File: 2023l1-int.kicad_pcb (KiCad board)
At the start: 2 copper layers, 185 x 188.1 mm, 134 parts, among them IC1 STM32F103CBTx, IC2 SN74LVC2G04DBVTG4, IC3 SN74LVC2G04DBVTG4, J1 52610-1433, J2 XT30, J3 PGMR, J4 FL, J5 FR, J6 BL, J7 BR, J8 XT60, Q1 STP75NF75, Q2 AO3400A, SW1 STM RST, SW2 L SW, SW3 M SW, U2 CD74HC4067SM, U4 CD74HC4067SM, U5 VNH5050A-E, U6 VNH5050A-E, U7 VNH5050A-E, U8 VNH5050A-E, Y1 8Mhz

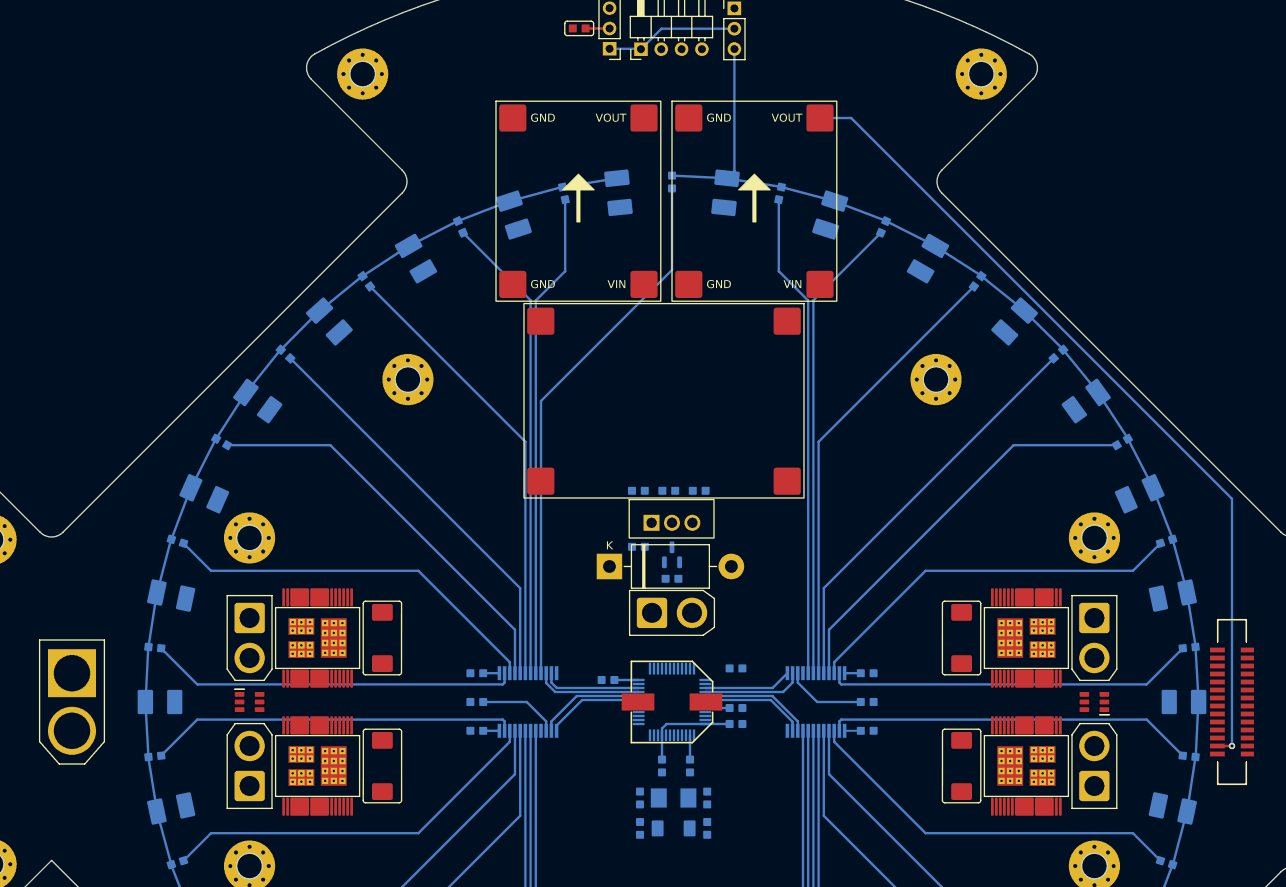
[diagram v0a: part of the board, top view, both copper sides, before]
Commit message: stm32 wiring done
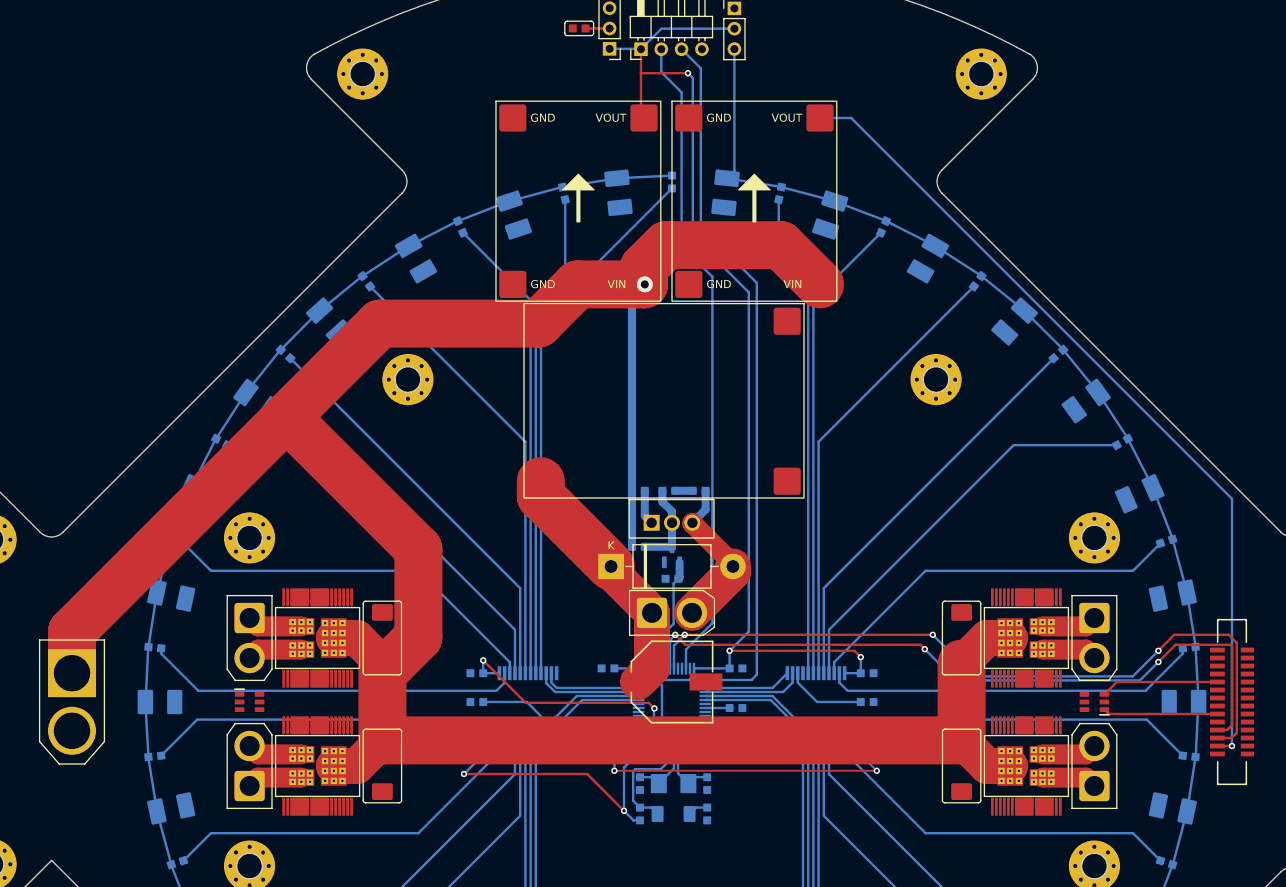
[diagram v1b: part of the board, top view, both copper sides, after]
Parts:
- moved C11 2.50 mm to (113.7, 103.5), turned to 0 degrees
- moved C14 2.37 mm to (110.7, 112.4), turned to 180 degrees
- moved D3 1.86 mm to (116.7, 112.3), turned to 180 degrees
- moved C4 1.80 mm to (118.1, 116.2)
- moved C5 1.80 mm to (109.7, 116.2)
- moved R41 1.80 mm to (118.1, 120.0)
- moved R45 1.80 mm to (109.7, 120.0)
- moved SW1 1.80 mm to (113.9, 120.0)
- moved Y1 1.80 mm to (113.9, 116.2)
- moved C12 1.45 mm to (105.7, 101.8)
- moved D2 0.20 mm to (106.1, 89.1)
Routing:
- net +12V: track 0.00 -> 316.8 mm, vias 0 -> 1
- net +3V3: track 36.3 -> 208.6 mm, vias 0 -> 5
- net /TX: track 0.00 -> 92.5 mm, vias 0 -> 3
- net /RX: track 0.00 -> 90.3 mm, vias 0 -> 3
- net /SWCLK: track 0.00 -> 88.8 mm
- net /SWDIO: track 0.00 -> 81.9 mm
- net /M1: track 2.03 -> 49.2 mm, vias 0 -> 2
- net +48V: track 0.00 -> 31.6 mm
- net /M2: track 2.02 -> 30.9 mm, vias 0 -> 2
- net Net-(D2-A): track 0.00 -> 20.2 mm
- net /RST: track 0.00 -> 15.7 mm
- net /BL DIR: track 0.00 -> 14.8 mm
- net /FL DIR: track 0.00 -> 14.4 mm
- net /Sol: track 0.00 -> 14.0 mm
- net Net-(Q2-D): track 0.00 -> 11.0 mm
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
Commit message: time to do it again
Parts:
- removed C16, C17, C18, C19: 220u, footprints:EIA-7343-D
- removed J4: FL, footprints:AMASS_XT30-F
- removed J5: FR, footprints:AMASS_XT30-F
- removed J6: BL, footprints:AMASS_XT30-F
- removed J7: BR, footprints:AMASS_XT30-F
- removed SW2: L SW, Connector_PinHeader_2.54mm:PinHeader_1x03_P2.54mm_Vertical
- removed U5, U6, U7, U8: VNH5050A-E, footprints:SOP50P1030X247-39N
- moved IC2 109.0 mm to (169.1, 119.0), turned to -90 degrees
- moved J1 14.7 mm to (169.0, 106.0)
- moved R41 13.8 mm to (104.3, 120.0), turned to 180 degrees
- moved IC3 13.3 mm to (169.1, 93.0), turned to 90 degrees
- moved R45 6.72 mm to (104.3, 116.0), turned to 0 degrees
- moved SW1 6.14 mm to (108.1, 118.0), turned to 90 degrees
- moved C13 6.05 mm to (116.4, 98.8), turned to 90 degrees
- moved C4 4.57 mm to (115.9, 120.2), turned to 180 degrees
- moved C5 4.57 mm to (111.9, 120.2), turned to 0 degrees
- moved R33 4.13 mm to (120.9, 110.8)
- moved Boost1 2.80 mm to (112.7, 65.6)
- moved U1 2.80 mm to (102.0, 40.6)
- moved U3 2.80 mm to (124.0, 40.6)
- moved J2 2.26 mm to (113.7, 92.6)
- moved C11 2.10 mm to (113.7, 101.4)
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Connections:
- D10 pad 2: VCC -> +3V3
- D11 pad 2: VCC -> +3V3
- D12 pad 2: VCC -> +3V3
- D13 pad 2: VCC -> +3V3
- D14 pad 2: VCC -> +3V3
- D15 pad 2: VCC -> +3V3
- D16 pad 2: VCC -> +3V3
- D17 pad 2: VCC -> +3V3
- D18 pad 2: VCC -> +3V3
- D19 pad 2: VCC -> +3V3
- D20 pad 2: VCC -> +3V3
- D21 pad 2: VCC -> +3V3
- D22 pad 2: VCC -> +3V3
- D23 pad 2: VCC -> +3V3
- D24 pad 2: VCC -> +3V3
- D25 pad 2: VCC -> +3V3
- D26 pad 2: VCC -> +3V3
- D27 pad 2: VCC -> +3V3
- D28 pad 2: VCC -> +3V3
- D29 pad 2: VCC -> +3V3
- D30 pad 2: VCC -> +3V3
- D31 pad 2: VCC -> +3V3
- D32 pad 2: VCC -> +3V3
- D33 pad 2: VCC -> +3V3
- D34 pad 2: VCC -> +3V3
- D5 pad 2: VCC -> +3V3
- D6 pad 2: VCC -> +3V3
- D7 pad 2: VCC -> +3V3
- D8 pad 2: VCC -> +3V3
- D9 pad 2: VCC -> +3V3
- IC1 pad 10: /M1 -> unconnected-(IC1-PA0-Pad10)
- IC1 pad 11: /M2 -> unconnected-(IC1-PA1-Pad11)
- IC1 pad 16: unconnected-(IC1-PA6-Pad16) -> /M1
- IC1 pad 17: unconnected-(IC1-PA7-Pad17) -> /S3
- IC1 pad 18: unconnected-(IC1-PB0-Pad18) -> /S2
- IC1 pad 19: /S3 -> /M2
- IC1 pad 20: /S2 -> /S0
- IC1 pad 21: /S0 -> /S1
- IC1 pad 22: /S1 -> unconnected-(IC1-PB11-Pad22)
- IC1 pad 39: /M1 S3 -> unconnected-(IC1-PB3-Pad39)
- IC1 pad 40: /M1 S2 -> /M1 S3
- IC1 pad 41: /M1 S0 -> /M1 S2
- IC1 pad 42: /M1 S1 -> /M1 S0
- IC1 pad 43: unconnected-(IC1-PB7-Pad43) -> /M1 S1
- IC2 pad 1: /BR DIR -> /FR DIR
- IC2 pad 3: /FR DIR -> /FL DIR
- IC2 pad 4: /!FR DIR -> /!FL DIR
- IC2 pad 6: /!BR DIR -> /!FR DIR
- IC3 pad 1: /FL DIR -> /BR DIR
- IC3 pad 6: /!FL DIR -> /!BR DIR
- R1 pad 1: VCC -> +3V3
- R10 pad 1: VCC -> +3V3
- R11 pad 1: VCC -> +3V3
- R12 pad 1: VCC -> +3V3
- R13 pad 1: VCC -> +3V3
- R14 pad 1: VCC -> +3V3
- R15 pad 1: VCC -> +3V3
- R16 pad 1: VCC -> +3V3
- R17 pad 1: VCC -> +3V3
- R18 pad 1: VCC -> +3V3
- R19 pad 1: VCC -> +3V3
- R2 pad 1: VCC -> +3V3
- R20 pad 1: VCC -> +3V3
- R21 pad 1: VCC -> +3V3
- R22 pad 1: VCC -> +3V3
- R23 pad 1: VCC -> +3V3
- R24 pad 1: VCC -> +3V3
- R25 pad 1: VCC -> +3V3
- R26 pad 1: VCC -> +3V3
- R27 pad 1: VCC -> +3V3
- R28 pad 1: VCC -> +3V3
- R29 pad 1: VCC -> +3V3
- R3 pad 1: VCC -> +3V3
- R30 pad 1: VCC -> +3V3
- R4 pad 1: VCC -> +3V3
- R5 pad 1: VCC -> +3V3
- R6 pad 1: VCC -> +3V3
- R7 pad 1: VCC -> +3V3
- R8 pad 1: VCC -> +3V3
- R9 pad 1: VCC -> +3V3
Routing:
- net VCC: track 423.0 -> 0.00 mm
- net +12V: track 316.8 -> 0.00 mm, vias 1 -> 0
- net +3V3: track 208.6 -> 24.3 mm, vias 5 -> 1
- net +5V: track 103.8 -> 3.40 mm
- net Net-(U4-I0): track 67.4 -> 0.00 mm
- net Net-(U2-I0): track 67.4 -> 0.00 mm
- net Net-(U4-I14): track 60.7 -> 0.00 mm
- net Net-(U4-I1): track 60.7 -> 0.00 mm
- net Net-(U2-I14): track 60.7 -> 0.00 mm
- net Net-(U2-I1): track 60.7 -> 0.00 mm
- net Net-(U4-I2): track 58.5 -> 0.00 mm
- net Net-(U2-I13): track 58.5 -> 0.00 mm
- net Net-(U4-I13): track 58.5 -> 0.00 mm
- net Net-(U2-I2): track 58.5 -> 0.00 mm
- net Net-(U4-I12): track 56.4 -> 0.00 mm
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- removed copper zone on B.Cu, net GND
- removed copper zone on F.Cu, net GND

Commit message: transitioning
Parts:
- added C16: 220u, footprints:EIA-7343-D, F.Cu at (146.5, 116.0)
- added C17: 220u, footprints:EIA-7343-D, F.Cu at (80.9, 116.0)
- added C18: 220u, footprints:EIA-7343-D, F.Cu at (146.5, 96.0)
- added C19: 220u, footprints:EIA-7343-D, F.Cu at (80.9, 96.0)
- added J4: FL, footprints:AMASS_XT30-F, F.Cu at (163.7, 116.0)
- added J5: FR, footprints:AMASS_XT30-F, F.Cu at (63.7, 116.0)
- added J6: BL, footprints:AMASS_XT30-F, F.Cu at (163.7, 96.0)
- added J7: BR, footprints:AMASS_XT30-F, F.Cu at (63.7, 96.0)
- added U5: VNH5050A-E, footprints:SOP50P1030X247-39N, F.Cu at (154.7, 116.0)
- added U6: VNH5050A-E, footprints:SOP50P1030X247-39N, F.Cu at (72.7, 116.0)
- added U7: VNH5050A-E, footprints:SOP50P1030X247-39N, F.Cu at (154.7, 96.0)
- added U8: VNH5050A-E, footprints:SOP50P1030X247-39N, F.Cu at (72.7, 96.0)
- moved IC2 2.68 mm to (171.8, 119.0)
- moved IC3 2.68 mm to (171.8, 93.0)
- moved J1 2.68 mm to (171.7, 106.0)
- moved C14 0.35 mm to (112.1, 113.2)
- moved J2 0.20 mm to (113.7, 92.8)
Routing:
- net +3V3: track 24.3 -> 438.5 mm
- net /M SW: track 0.00 -> 98.0 mm, vias 0 -> 8
- net +48V: track 0.00 -> 32.3 mm
- net /!FL DIR: track 0.00 -> 27.9 mm, vias 0 -> 2
- net /FL DIR: track 11.4 -> 34.2 mm
- net /FL PWM: track 0.00 -> 21.2 mm, vias 0 -> 2
- net Net-(D2-A): track 0.00 -> 20.1 mm
- net /Sol: track 0.74 -> 16.0 mm
- net Net-(Q2-D): track 0.00 -> 11.0 mm
- net Net-(U4-~{E}): track 0.00 -> 10.0 mm
- net +12V: track 0.00 -> 7.00 mm
- net Net-(Q1-Pad1): track 0.00 -> 4.35 mm
- net /RX: track 60.3 -> 63.9 mm
- net /SWDIO: track 89.8 -> 86.5 mm
- net /TX: track 60.5 -> 63.7 mm
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- added copper zone on B.Cu, net GND
- added copper zone on F.Cu, net GND

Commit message: fl and fr done
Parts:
- turned C16 to 90 degrees
- turned C19 to -90 degrees
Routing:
- net +12V: track 7.00 -> 184.9 mm, vias 0 -> 1
- net /M SW: track 98.0 -> 259.3 mm, vias 8 -> 10
- net /!FR DIR: track 0.00 -> 120.3 mm, vias 0 -> 2
- net /FR PWM: track 0.00 -> 115.0 mm, vias 0 -> 2
- net /FR DIR: track 14.1 -> 117.8 mm
- net +3V3: track 438.5 -> 455.9 mm
- net /FR B: track 0.00 -> 7.41 mm
- net /BR B: track 0.00 -> 7.41 mm
- net /FL A: track 0.00 -> 7.41 mm
- net /BL A: track 0.00 -> 7.41 mm
- net /FR A: track 0.00 -> 7.41 mm
- net /BR A: track 0.00 -> 7.41 mm
- net /FL B: track 0.00 -> 7.41 mm
- net /BL B: track 0.00 -> 7.41 mm

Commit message: left with msw
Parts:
- moved C11 34.4 mm to (89.7, 76.8), turned to -90 degrees
- moved R33 3.60 mm to (118.2, 113.2), turned to 90 degrees
- moved C16 0.80 mm to (145.7, 116.0), turned to -90 degrees
- moved C18 0.80 mm to (145.7, 96.0), turned to 90 degrees
- moved C19 0.80 mm to (81.7, 96.0), turned to 90 degrees
- moved C17 0.80 mm to (81.7, 116.0), turned to -90 degrees
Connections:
- IC1 pad 12: unconnected-(IC1-PA2-Pad12) -> /TX
- IC1 pad 13: unconnected-(IC1-PA3-Pad13) -> /RX
- IC1 pad 30: /RX -> unconnected-(IC1-PA9-Pad30)
- IC1 pad 31: /TX -> unconnected-(IC1-PA10-Pad31)
- U5 pad 15: /!FL DIR -> /FL DIR
- U5 pad 22: /FL DIR -> /!FL DIR
- U6 pad 15: /FR DIR -> /!FR DIR
- U6 pad 22: /!FR DIR -> /FR DIR
- U7 pad 15: /BL DIR -> /!BL DIR
- U7 pad 22: /!BL DIR -> /BL DIR
- U8 pad 15: /!BR DIR -> /BR DIR
- U8 pad 22: /BR DIR -> /!BR DIR
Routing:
- net /M SW: track 259.3 -> 0.00 mm, vias 10 -> 0
- net +12V: track 184.9 -> 374.9 mm
- net +3V3: track 455.9 -> 632.8 mm, vias 1 -> 8
- net +5V: track 2.11 -> 115.9 mm, vias 1 -> 2
- net /BR DIR: track 11.4 -> 114.2 mm, vias 0 -> 4
- net /!BR DIR: track 0.00 -> 97.6 mm, vias 0 -> 2
- net /BR PWM: track 0.00 -> 95.1 mm, vias 0 -> 2
- net Net-(U4-I0): track 0.00 -> 67.4 mm
- net Net-(U2-I0): track 0.00 -> 67.4 mm
- net Net-(U4-I14): track 0.00 -> 60.7 mm
- net Net-(U4-I1): track 0.00 -> 60.7 mm
- net Net-(U2-I14): track 0.00 -> 60.7 mm
- net Net-(U2-I1): track 0.00 -> 60.7 mm
- net Net-(U4-I2): track 0.00 -> 58.5 mm
- net Net-(U2-I13): track 0.00 -> 58.5 mm
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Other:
- outline, holes or cut-outs redrawn

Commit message: done
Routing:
- net /M SW: track 0.00 -> 250.9 mm, vias 0 -> 17
- net +3V3: track 632.8 -> 658.3 mm
- net /FR PWM: track 101.7 -> 104.7 mm
- net /BR PWM: track 95.1 -> 96.8 mm
- net /BR DIR: track 114.2 -> 115.0 mm

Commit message: done
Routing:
- net +3V3: track 658.3 -> 644.2 mm
- net /M SW: vias 17 -> 16

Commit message: done
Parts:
- moved C11 24.6 mm to (103.7, 97.0)
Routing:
- net /BR DIR: track 115.0 -> 117.0 mm
- net +48V: track 31.8 -> 30.5 mm
- net /M SW: track 250.9 -> 251.5 mm
- net +12V: track 374.9 -> 375.5 mm
